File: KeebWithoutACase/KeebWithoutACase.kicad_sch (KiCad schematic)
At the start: 133 parts, among them SW1 SW_Push_45deg, SW10 SW_Push_45deg, SW11 SW_Push_45deg, SW12 SW_Push_45deg, SW13 SW_Push_45deg, SW14 SW_Push_45deg, SW15 SW_Push_45deg, SW16 SW_Push_45deg, SW17 SW_Push_45deg, SW18 SW_Push_45deg, SW19 SW_Push_45deg, SW2 SW_Push_45deg, SW20 SW_Push_45deg, SW21 SW_Push_45deg, SW22 SW_Push_45deg, SW23 SW_Push_45deg, SW24 SW_Push_45deg, SW25 SW_Push_45deg, SW26 SW_Push_45deg, SW27 SW_Push_45deg, SW28 SW_Push_45deg, SW29 SW_Push_45deg, SW3 SW_Push_45deg, SW30 SW_Push_45deg, SW31 SW_Push_45deg, SW32 SW_Push_45deg, SW33 SW_Push_45deg, SW34 SW_Push_45deg, SW35 SW_Push_45deg, SW36 SW_Push_45deg, SW37 SW_Push_45deg, SW38 SW_Push_45deg, SW39 SW_Push_45deg, SW4 SW_Push_45deg, SW40 SW_Push_45deg, SW41 SW_Push_45deg, SW42 SW_Push_45deg, SW43 SW_Push_45deg, SW44 SW_Push_45deg, SW45 SW_Push_45deg, SW46 SW_Push_45deg, SW47 SW_Push_45deg, SW48 SW_Push_45deg, SW49 SW_Push_45deg, SW5 SW_Push_45deg, SW50 SW_Push_45deg, SW51 SW_Push_45deg, SW52 SW_Push_45deg, SW53 SW_Push_45deg, SW54 SW_Push_45deg, SW56 SW_Push_45deg, SW57 SW_Push_45deg, SW58 SW_Push_45deg, SW59 SW_Push_45deg, SW6 SW_Push_45deg, SW60 SW_Push_45deg, SW61 SW_Push_45deg, SW62 SW_Push_45deg, SW63 SW_Push_45deg, SW64 SW_Push_45deg, SW65 SW_Push_45deg, SW66 SW_Push_45deg, SW67 SW_Push_45deg, SW7 SW_Push_45deg, SW8 SW_Push_45deg, SW9 SW_Push_45deg

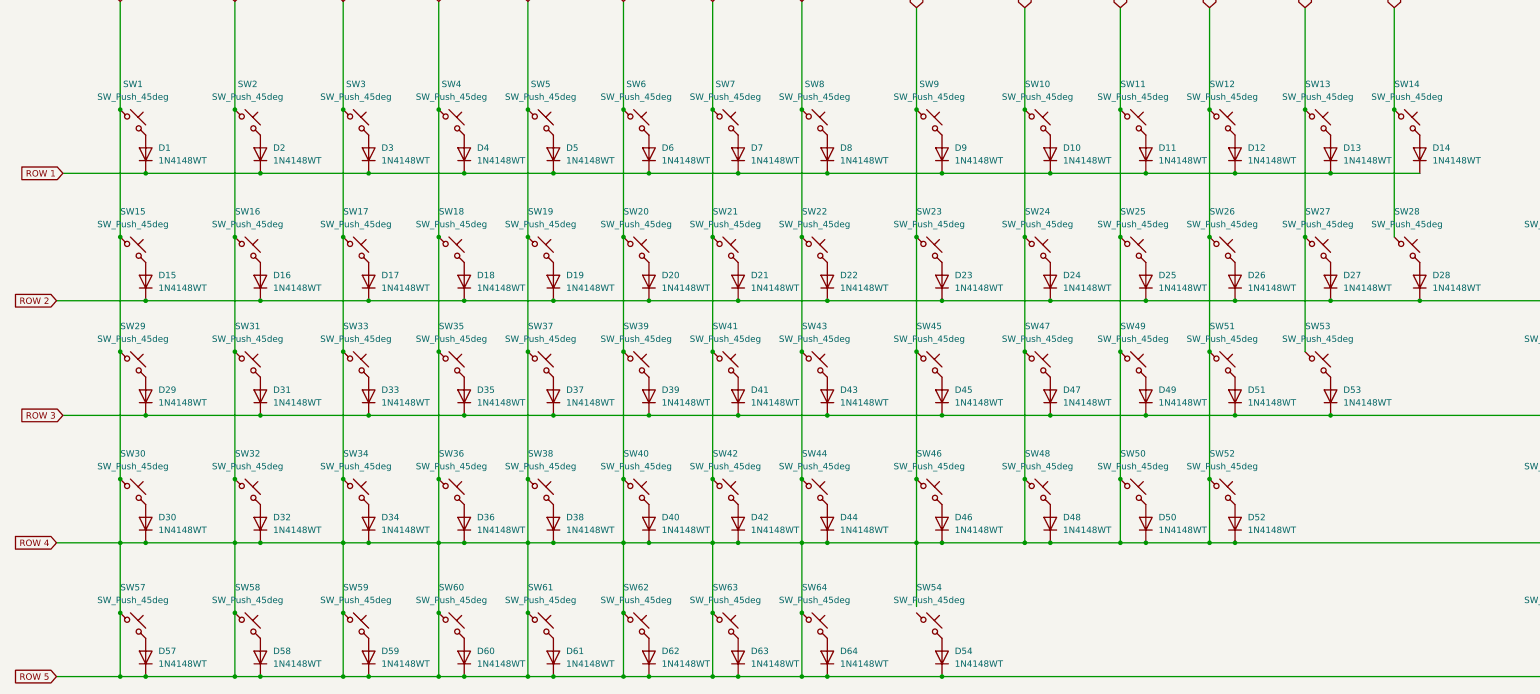
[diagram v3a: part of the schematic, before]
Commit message: assigned all the diode footprint and maximum footpprints for the siwtches
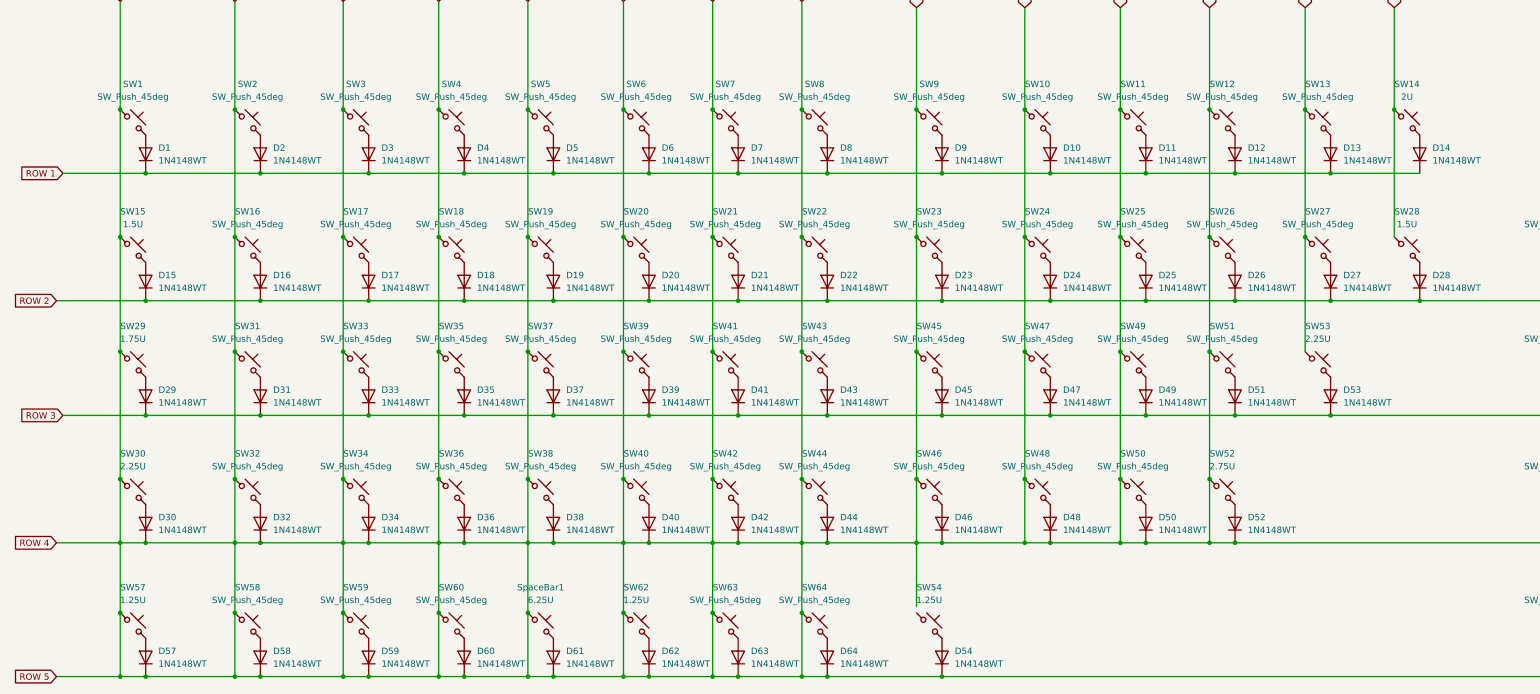
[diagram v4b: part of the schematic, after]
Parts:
- D1: footprint Diode_SMD:D_SOD-523 -> Diode_THT:D_DO-27_P15.24mm_Horizontal
- RV1: footprint (none) -> Potentiometer_THT:Potentiometer_ACP_CA6-H2,5_Horizontal
- SW1, SW10, SW11, SW12, SW13, SW16, SW17, SW18, SW19, SW2, SW20, SW21, SW22, SW23, SW24, SW25, SW26, SW27, SW3, SW31, SW32, SW33, SW34, SW35, SW36, SW37, SW38, SW39, SW4, SW40, SW41, SW42, SW43, SW44, SW45, SW46, SW47, SW48, SW49, SW5, SW50, SW51, SW56, SW58, SW59, SW6, SW60, SW63, SW64, SW65, SW66, SW67, SW7, SW8, SW9: footprint (none) -> Button_Switch_Keyboard:SW_Cherry_MX_1.00u_PCB
- SW14: value SW_Push_45deg -> 2U; footprint (none) -> Button_Switch_Keyboard:SW_Cherry_MX_1.00u_PCB
- SW15, SW28: value SW_Push_45deg -> 1.5U; footprint (none) -> Button_Switch_Keyboard:SW_Cherry_MX_1.00u_PCB
- SW29: value SW_Push_45deg -> 1.75U; footprint (none) -> Button_Switch_Keyboard:SW_Cherry_MX_1.00u_PCB
- SW30, SW53: value SW_Push_45deg -> 2.25U; footprint (none) -> Button_Switch_Keyboard:SW_Cherry_MX_1.00u_PCB
- SW52: value SW_Push_45deg -> 2.75U; footprint (none) -> Button_Switch_Keyboard:SW_Cherry_MX_1.00u_PCB
- SW54, SW57, SW62: value SW_Push_45deg -> 1.25U; footprint (none) -> Button_Switch_Keyboard:SW_Cherry_MX_1.00u_PCB
- SpaceBar1: renamed from SW61; value SW_Push_45deg -> 6.25U; footprint (none) -> Button_Switch_Keyboard:SW_Cherry_MX_1.00u_PCB

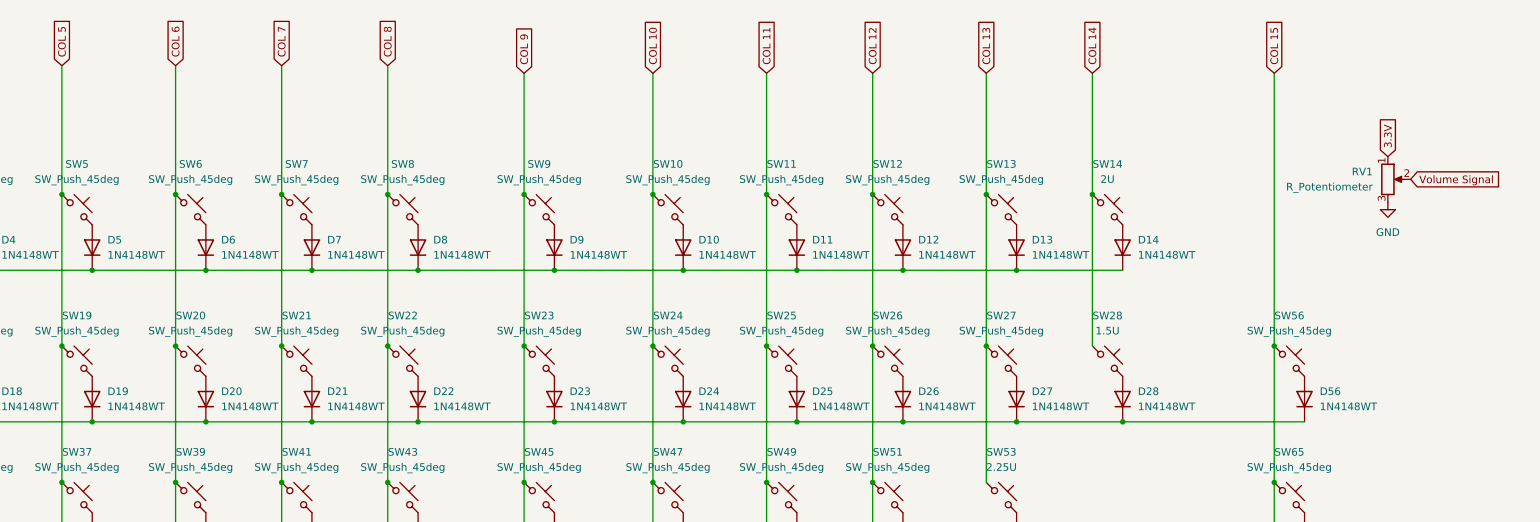
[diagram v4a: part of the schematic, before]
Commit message: replaced the potentiometer with a rotary encoder and fixed all the footprints for the diodes to be compatible with the ones available near me
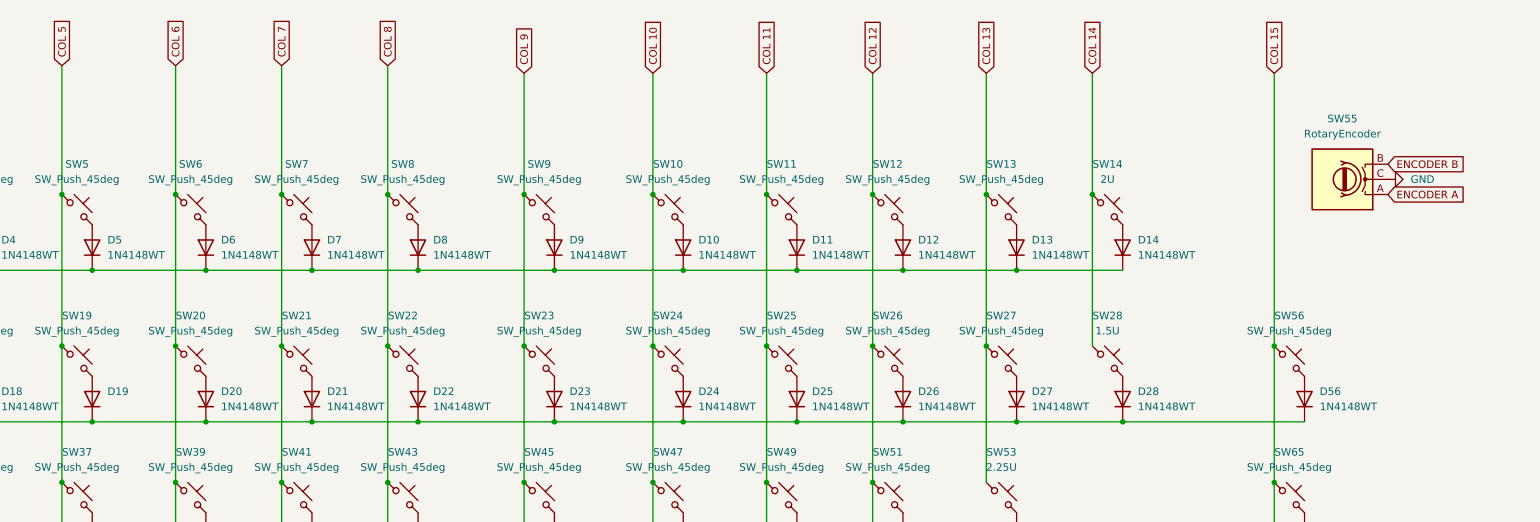
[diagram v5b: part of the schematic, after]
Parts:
- removed RV1: R_Potentiometer, Potentiometer_THT:Potentiometer_ACP_CA6-H2,5_Horizontal, symbol Device:R_Potentiometer
- added SW55: RotaryEncoder, symbol Device:RotaryEncoder
- D10, D11, D12, D13, D14, D15, D16, D17, D18, D2, D20, D21, D22, D23, D24, D25, D26, D27, D28, D29, D3, D30, D31, D32, D33, D34, D35, D36, D37, D38, D39, D4, D40, D41, D42, D43, D44, D45, D46, D47, D48, D49, D5, D50, D51, D52, D53, D54, D56, D57, D58, D59, D6, D60, D61, D62, D63, D64, D65, D66, D67, D7, D8, D9: footprint Diode_SMD:D_SOD-523 -> Diode_THT:D_DO-27_P15.24mm_Horizontal
- D19: value 1N4148WT -> ~; footprint Diode_SMD:D_SOD-523 -> Diode_THT:D_DO-27_P15.24mm_Horizontal
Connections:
- net GND: now also SW55.C
- new net ENCODER A: SW55.A
- new net ENCODER B: SW55.B

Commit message: adjustedd the footprint to match the size of the cherry keys in the schem
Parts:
- SW14: footprint Button_Switch_Keyboard:SW_Cherry_MX_1.00u_PCB -> Button_Switch_Keyboard:SW_Cherry_MX_2.00u_PCB
- SW15, SW28: footprint Button_Switch_Keyboard:SW_Cherry_MX_1.00u_PCB -> Button_Switch_Keyboard:SW_Cherry_MX_1.50u_PCB
- SW29: footprint Button_Switch_Keyboard:SW_Cherry_MX_1.00u_PCB -> Button_Switch_Keyboard:SW_Cherry_MX_1.75u_PCB
- SW30, SW53: footprint Button_Switch_Keyboard:SW_Cherry_MX_1.00u_PCB -> Button_Switch_Keyboard:SW_Cherry_MX_2.25u_PCB
- SW52: footprint Button_Switch_Keyboard:SW_Cherry_MX_1.00u_PCB -> Button_Switch_Keyboard:SW_Cherry_MX_2.75u_PCB
- SW54, SW57, SW62: footprint Button_Switch_Keyboard:SW_Cherry_MX_1.00u_PCB -> Button_Switch_Keyboard:SW_Cherry_MX_1.25u_PCB
- SW55: footprint (none) -> Rotary_Encoder:RotaryEncoder_Alps_EC11E-Switch_Vertical_H20mm
- SpaceBar1: footprint Button_Switch_Keyboard:SW_Cherry_MX_1.00u_PCB -> Button_Switch_Keyboard:SW_Cherry_MX_6.25u_PCB
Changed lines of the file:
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@@
 			)
 		)
-		(property "Footprint" "Button_Switch_Keyboard:SW_Cherry_MX_1.00u_PCB"
+		(property "Footprint" "Button_Switch_Keyboard:SW_Cherry_MX_2.25u_PCB"
 			(at 309.88 111.76 0)
 			(effects
@@
 			)
 		)
-		(property "Footprint" "Button_Switch_Keyboard:SW_Cherry_MX_1.00u_PCB"
+		(property "Footprint" "Button_Switch_Keyboard:SW_Cherry_MX_1.25u_PCB"
 			(at 73.66 163.83 0)
 			(effects
@@
 			)
 		)
-		(property "Footprint" "Button_Switch_Keyboard:SW_Cherry_MX_1.00u_PCB"
+		(property "Footprint" "Button_Switch_Keyboard:SW_Cherry_MX_1.25u_PCB"
 			(at 173.99 163.83 0)
 			(effects
@@
 			)
 		)
-		(property "Footprint" "Button_Switch_Keyboard:SW_Cherry_MX_1.00u_PCB"
+		(property "Footprint" "Button_Switch_Keyboard:SW_Cherry_MX_1.50u_PCB"
 			(at 327.66 88.9 0)
 			(effects
@@
 			)
 		)
-		(property "Footprint" "Button_Switch_Keyboard:SW_Cherry_MX_1.00u_PCB"
+		(property "Footprint" "Button_Switch_Keyboard:SW_Cherry_MX_1.50u_PCB"
 			(at 73.66 88.9 0)
 			(effects
@@
 			)
 		)
-		(property "Footprint" "Button_Switch_Keyboard:SW_Cherry_MX_1.00u_PCB"
+		(property "Footprint" "Button_Switch_Keyboard:SW_Cherry_MX_6.25u_PCB"
 			(at 154.94 163.83 0)
 			(effects
@@
 			)
 		)
-		(property "Footprint" "Button_Switch_Keyboard:SW_Cherry_MX_1.00u_PCB"
+		(property "Footprint" "Button_Switch_Keyboard:SW_Cherry_MX_1.25u_PCB"
 			(at 232.41 163.83 0)
 			(effects
@@
 			)
 		)
-		(property "Footprint" "Button_Switch_Keyboard:SW_Cherry_MX_1.00u_PCB"
+		(property "Footprint" "Button_Switch_Keyboard:SW_Cherry_MX_1.75u_PCB"
 			(at 73.66 111.76 0)
 			(effects
@@
 			)
 		)
-		(property "Footprint" ""
+		(property "Footprint" "Rotary_Encoder:RotaryEncoder_Alps_EC11E-Switch_Vertical_H20mm"
 			(at 370.84 62.484 0)
 			(effects
@@
 			)
 		)
-		(property "Footprint" "Button_Switch_Keyboard:SW_Cherry_MX_1.00u_PCB"
+		(property "Footprint" "Button_Switch_Keyboard:SW_Cherry_MX_2.75u_PCB"
 			(at 290.83 137.16 0)
 			(effects
@@
 			)
 		)
-		(property "Footprint" "Button_Switch_Keyboard:SW_Cherry_MX_1.00u_PCB"
+		(property "Footprint" "Button_Switch_Keyboard:SW_Cherry_MX_2.00u_PCB"
 			(at 327.66 63.5 0)
 			(effects
@@
 			)
 		)
-		(property "Footprint" "Button_Switch_Keyboard:SW_Cherry_MX_1.00u_PCB"
+		(property "Footprint" "Button_Switch_Keyboard:SW_Cherry_MX_2.25u_PCB"
 			(at 73.66 137.16 0)
 			(effects

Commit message: wired the keeb matrix onto an mcu in the schematic
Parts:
- added A1: RaspberryPi_Pico, Module:RaspberryPi_Pico_Common_Unspecified, symbol MCU_Module:RaspberryPi_Pico
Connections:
- net COL 1: now also A1.10 (GPIO7), A1.11 (GPIO8), A1.12 (GPIO9), A1.14 (GPIO10), A1.15 (GPIO11), A1.16 (GPIO12), A1.17 (GPIO13), A1.19 (GPIO14), A1.20 (GPIO15), A1.21 (GPIO16), A1.25 (GPIO19), A1.5 (GPIO3), A1.6 (GPIO4), A1.7 (GPIO5), A1.9 (GPIO6)
- net COL 13: now also A1.22 (GPIO17)
- net COL 14: now also A1.24 (GPIO18)
- net ENCODER A: now also A1.26 (GPIO20)
- net ENCODER B: now also A1.27 (GPIO21)
- net ROW 1: now also A1.1 (GPIO0)
- net ROW 2: now also A1.2 (GPIO1)
- net ROW 3: now also A1.4 (GPIO2)
- new net: A1.13 (GND), A1.18 (GND), A1.23 (GND), A1.28 (GND), A1.3 (GND), A1.38 (GND), A1.8 (GND)
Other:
- moved on the sheet: D1, D10, D11, D12, D13, D14, D15, D16, D17, D18, D19, D2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

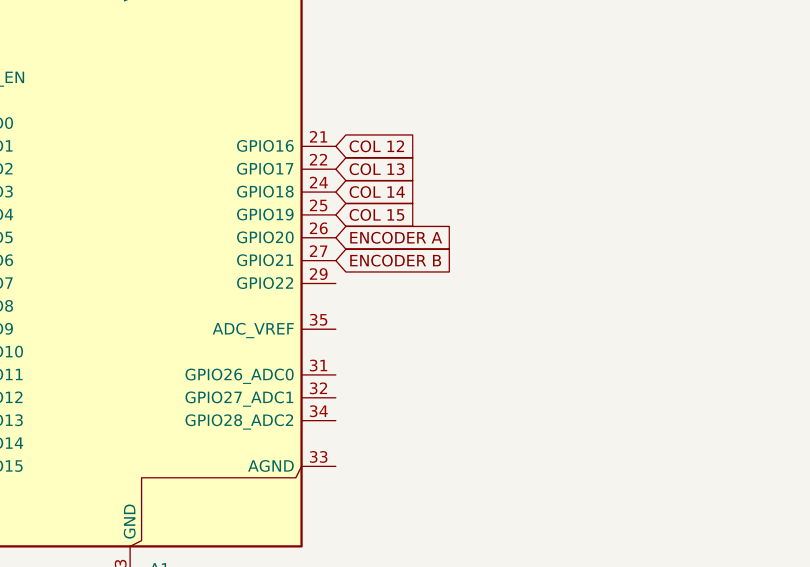
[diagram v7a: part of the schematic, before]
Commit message: completed the first row of keys
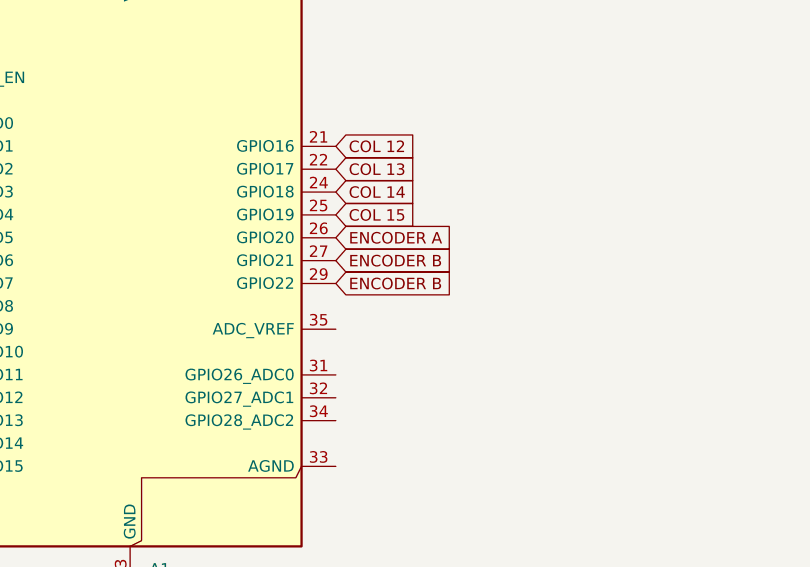
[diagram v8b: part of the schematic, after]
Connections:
- net ENCODER B: now also A1.29 (GPIO22)
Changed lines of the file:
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@@
+		)
+	)
+	(global_label "ENCODER B"
+		(shape input)
+		(at 73.66 63.5 0)
+		(fields_autoplaced yes)
+		(effects
+			(font
+				(size 1.27 1.27)
+			)
+			(justify left)
+		)
+		(property "Intersheetrefs" "${INTERSHEET_REFS}"
+			(at 87.6518 63.5 0)
+			(effects
+				(font
+					(size 1.27 1.27)
+				)
+				(justify left)
+				(hide yes)
+			)
 		)
 	)
